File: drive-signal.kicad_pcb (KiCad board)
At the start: 2 copper layers, 43.2 x 67.8 mm, 25 parts, among them J1 Conn_01x03_Pin, J10 Conn_01x04_Pin, J11 Conn_01x04_Pin, J2 Conn_01x03_Pin, J3 Conn_01x03_Pin, J4 Conn_01x03_Pin, J5 JETSON, J6 IMU, J7 Conn_01x02_Pin, J8 Conn_01x04_Pin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

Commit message: fix mount holes
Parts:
- added ?: , , F.Cu at (50.0, 31.5)
- added ?: , , F.Cu at (86.6, 61.2)
- added ?: , , F.Cu at (86.6, 31.5)
- added ?: , , F.Cu at (50.0, 60.7)
- added ?: , , F.Cu at (63.2, 93.0)
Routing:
- net (no net): vias 5 -> 0
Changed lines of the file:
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@@
     )
   )
+  (footprint "" (layer "F.Cu")
+    (at 50.038 31.496)
+    (fp_text reference "" (at 0 0) (layer "F.SilkS")
+        (effects (font (size 1.27 1.27) (thickness 0.15)))
+    )
+    (fp_text value "" (at 0 0) (layer "F.SilkS")
+        (effects (font (size 1.27 1.27) (thickness 0.15)))
+    )
+    (pad "1" thru_hole circle (at 0 0) (size 3.5 3.5) (drill 3.2) (layers "*.Cu" "*.Mask"))
+  )
   (footprint "Resistor_SMD:R_0805_2012Metric_Pad1.20x1.40mm_HandSolder" (layer "F.Cu")
     (at 64.77 62.23 180)
@@
     )
   )
+  (footprint "" (layer "F.Cu")
+    (at 86.614 61.214)
+    (fp_text reference "" (at 0 0) (layer "F.SilkS")
+        (effects (font (size 1.27 1.27) (thickness 0.15)))
+    )
+    (fp_text value "" (at 0 0) (layer "F.SilkS")
+        (effects (font (size 1.27 1.27) (thickness 0.15)))
+    )
+    (pad "1" thru_hole circle (at 0 0) (size 3.5 3.5) (drill 3.2) (layers "*.Cu" "*.Mask"))
+  )
   (footprint "Connector_JST:JST_PH_B3B-PH-K_1x03_P2.00mm_Vertical" (layer "F.Cu")
     (at 84.328 67.422 -90)
@@
     )
   )
+  (footprint "" (layer "F.Cu")
+    (at 86.614 31.496)
+    (fp_text reference "" (at 0 0) (layer "F.SilkS")
+        (effects (font (size 1.27 1.27) (thickness 0.15)))
+    )
+    (fp_text value "" (at 0 0) (layer "F.SilkS")
+        (effects (font (size 1.27 1.27) (thickness 0.15)))
+    )
+    (pad "1" thru_hole circle (at 0 0) (size 3.5 3.5) (drill 3.2) (layers "*.Cu" "*.Mask"))
+  )
   (footprint "LED_SMD:LED_0805_2012Metric_Pad1.15x1.40mm_HandSolder" (layer "F.Cu")
     (at 84.319 46.482 180)
@@
     )
   )
+  (footprint "" (layer "F.Cu")
+    (at 50.038 60.706)
+    (fp_text reference "" (at 0 0) (layer "F.SilkS")
+        (effects (font (size 1.27 1.27) (thickness 0.15)))
+    )
+    (fp_text value "" (at 0 0) (layer "F.SilkS")
+        (effects (font (size 1.27 1.27) (thickness 0.15)))
+    )
+    (pad "1" thru_hole circle (at 0 0) (size 3.5 3.5) (drill 3.2) (layers "*.Cu" "*.Mask"))
+  )
   (footprint "Resistor_SMD:R_0805_2012Metric_Pad1.20x1.40mm_HandSolder" (layer "F.Cu")
     (at 79.97 46.482)
@@
     )
   )
+  (footprint "" (layer "F.Cu")
+    (at 63.246 92.964)
+    (fp_text reference "" (at 0 0) (layer "F.SilkS")
+        (effects (font (size 1.27 1.27) (thickness 0.15)))
+    )
+    (fp_text value "" (at 0 0) (layer "F.SilkS")
+        (effects (font (size 1.27 1.27) (thickness 0.15)))
+    )
+    (pad "1" thru_hole circle (at 0 0) (size 3.5 3.5) (drill 3.2) (layers "*.Cu" "*.Mask"))
+  )
   (footprint "LED_SMD:LED_0805_2012Metric_Pad1.15x1.40mm_HandSolder" (layer "F.Cu")
     (at 84.319 75.438 180)
@@
     (effects (font (size 0.5 0.5) (thickness 0.1)) (justify left bottom))
   )
-  (via (at 63.246 92.964) (size 4) (drill 3.5) (layers "F.Cu" "B.Cu") (free) (net 0))
-  (via (at 86.614 31.496) (size 4) (drill 3.5) (layers "F.Cu" "B.Cu") (free) (net 0))
-  (via (at 50.038 60.706) (size 4) (drill 3.5) (layers "F.Cu" "B.Cu") (free) (net 0))
-  (via (at 86.614 61.214) (size 4) (drill 3.5) (layers "F.Cu" "B.Cu") (free) (net 0))
-  (via (at 50.038 31.496) (size 4) (drill 3.5) (layers "F.Cu" "B.Cu") (free) (net 0))
   (segment (start 59.992 75.438) (end 60.6334 74.7966) (width 1) (layer "F.Cu") (net 7))
   (segment (start 57.404 75.438) (end 57.404 72.373) (width 1) (layer "F.Cu") (net 7))

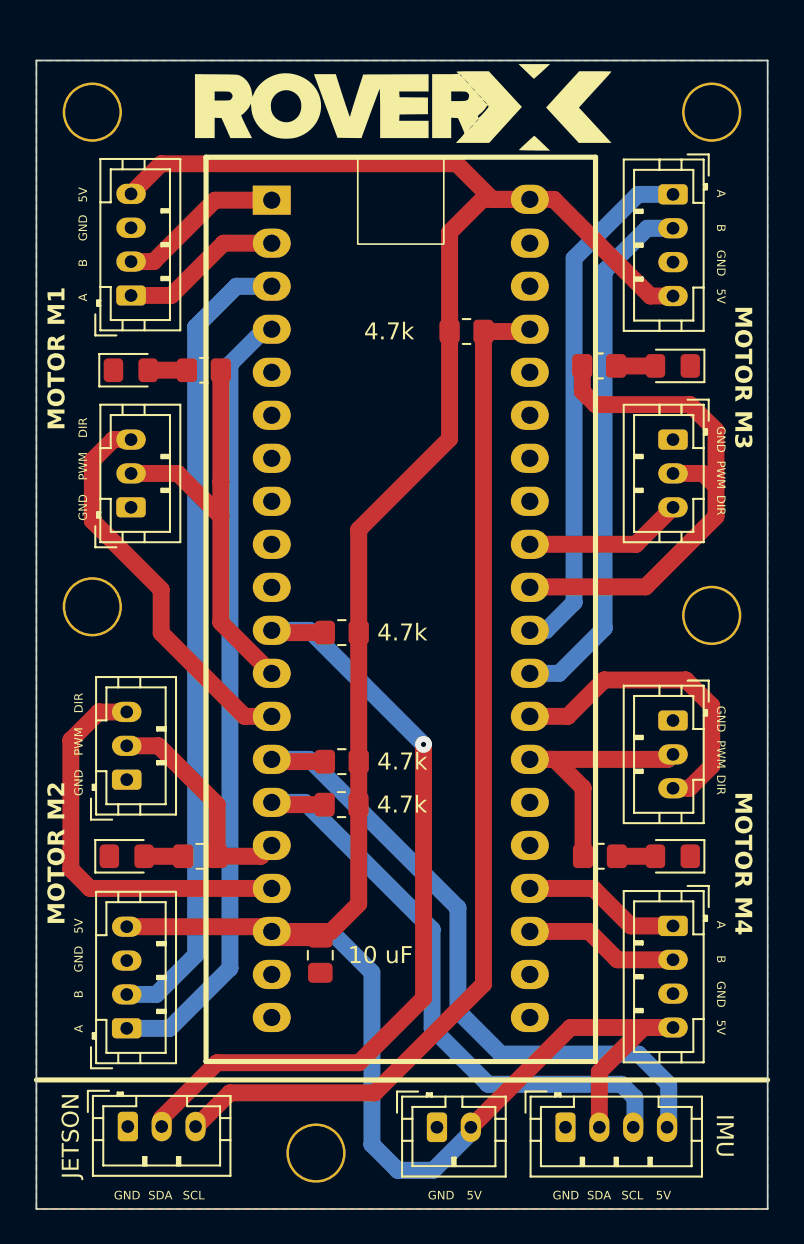
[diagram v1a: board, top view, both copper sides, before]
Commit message: make JSTs horizontal
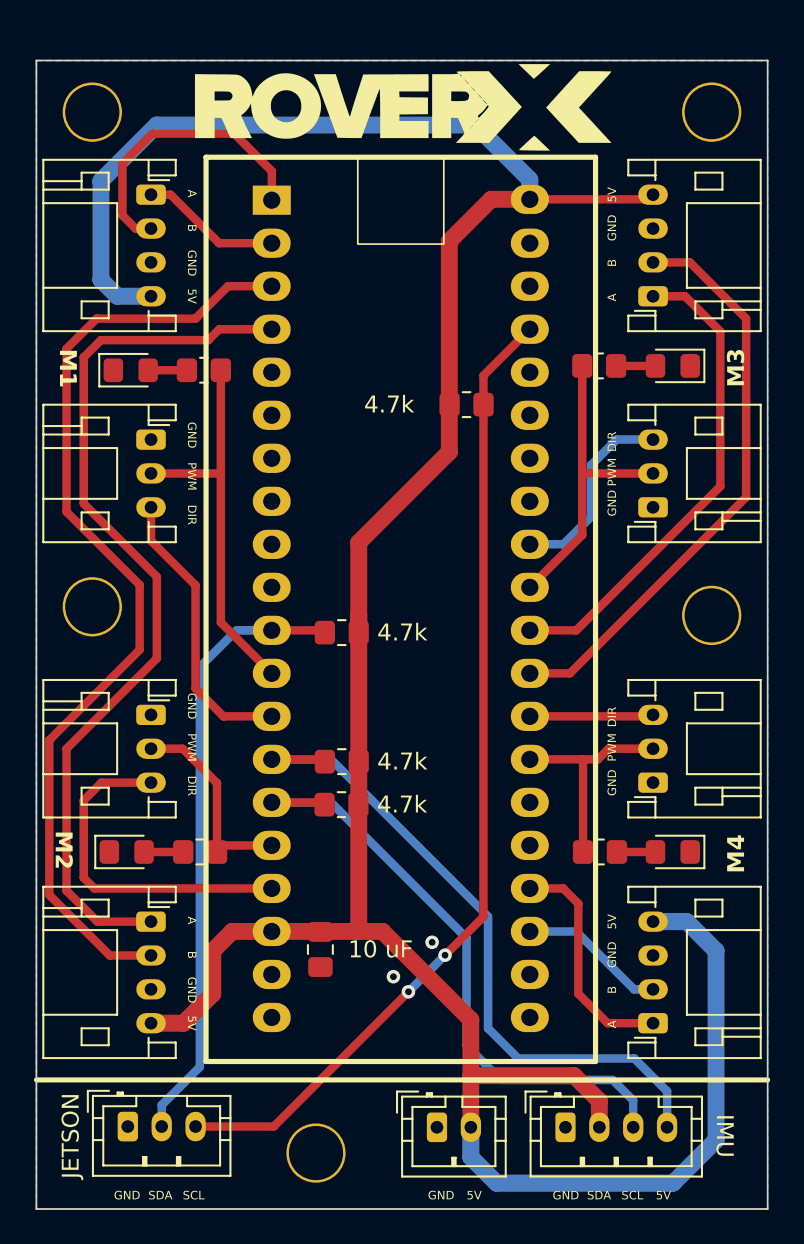
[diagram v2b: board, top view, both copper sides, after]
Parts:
- J1, J2, J3, J4: footprint Connector_JST:JST_PH_B3B-PH-K_1x03_P2.00mm_Vertical -> Connector_JST:JST_PH_S3B-PH-K_1x03_P2.00mm_Horizontal
- J10, J11, J8, J9: footprint Connector_JST:JST_PH_B4B-PH-K_1x04_P2.00mm_Vertical -> Connector_JST:JST_PH_S4B-PH-K_1x04_P2.00mm_Horizontal
- moved J9 6.46 mm to (53.5, 79.3), turned to -90 degrees
- moved J11 6.13 mm to (83.1, 42.4), turned to 90 degrees
- moved J8 6.07 mm to (53.5, 36.4), turned to -90 degrees
- moved J10 5.87 mm to (83.1, 85.3), turned to 90 degrees
- moved R4 4.32 mm to (72.1, 48.8)
- moved J4 4.17 mm to (83.1, 54.8), turned to 90 degrees
- moved J1 4.17 mm to (53.5, 50.8), turned to -90 degrees
- moved J2 4.09 mm to (53.5, 67.1), turned to -90 degrees
- moved J3 3.85 mm to (83.1, 71.1), turned to 90 degrees
- moved C1 0.34 mm to (63.5, 80.9)
- moved D1 0.25 mm to (52.1, 75.2)
- moved D3 0.25 mm to (84.3, 75.2)
- moved R5 0.25 mm to (56.4, 75.2)
- moved R7 0.25 mm to (80.0, 75.2)
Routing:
- net +5V: track 148.8 -> 170.0 mm
- net I2C2_J_SDA: track 49.1 -> 36.4 mm, vias 1 -> 0
- net PWM_RB: track 31.0 -> 18.5 mm
- net DIR_RF: track 19.2 -> 7.31 mm
- net LB_B: track 47.6 -> 57.4 mm
- net LF_B: track 9.81 -> 17.2 mm
- net LB_A: track 46.6 -> 53.0 mm
- net DIR_LF: track 23.2 -> 17.0 mm
- net RF_A: track 9.37 -> 13.7 mm
- net I2C2_J_SCL: track 62.1 -> 58.0 mm, vias 0 -> 2
- net DIR_LB: track 23.9 -> 20.3 mm
- net PWM_RF: track 16.5 -> 13.0 mm
- net RB_B: track 31.7 -> 34.5 mm
- net RB_A: track 31.0 -> 28.8 mm
- net DIR_RB: track 9.36 -> 11.6 mm
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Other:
- board text added: "M1"
- board text added: "M2"
- board text added: "M3"
- board text added: "M4"
- board text removed: "MOTOR M1"
- board text removed: "MOTOR M2"
- board text removed: "MOTOR M3"
- board text removed: "MOTOR M4"

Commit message: minor layout improvements
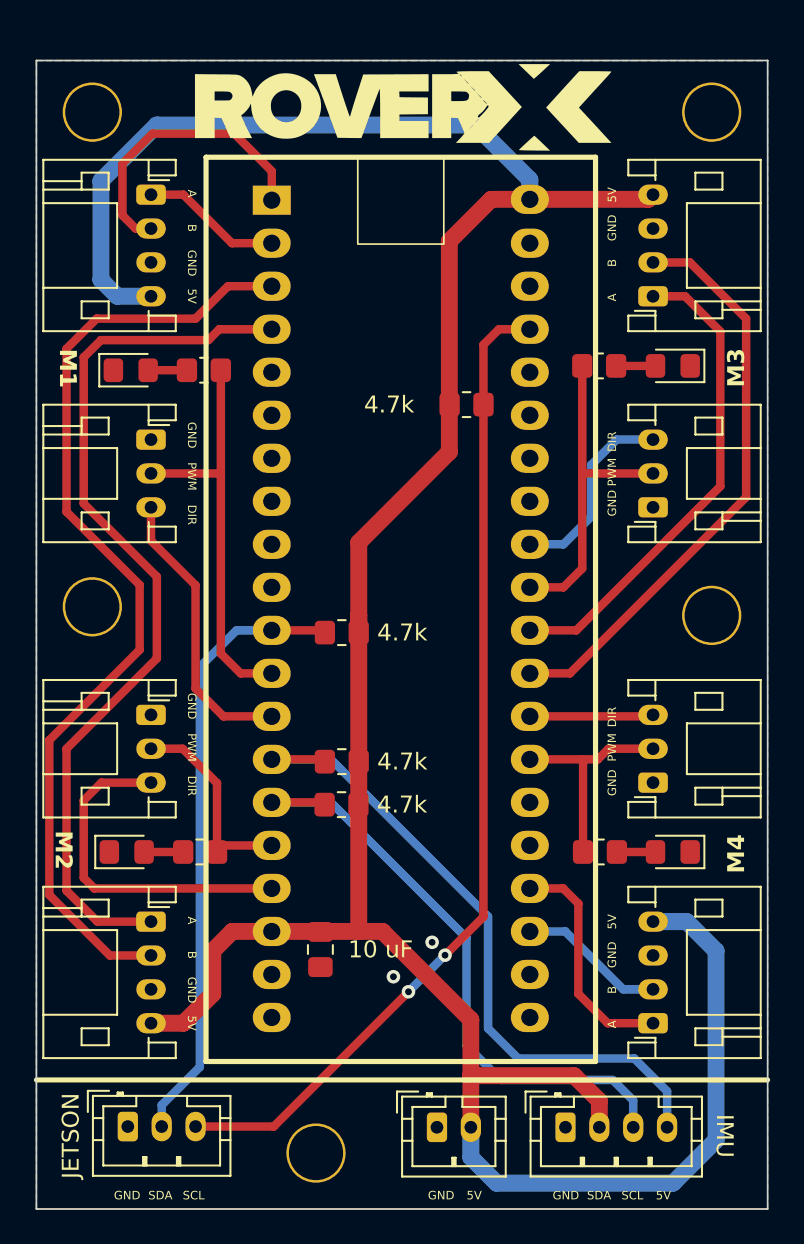
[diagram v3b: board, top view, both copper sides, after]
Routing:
- net PWM_RB: track 18.5 -> 19.7 mm
- net PWM_LF: track 23.3 -> 24.3 mm
- net I2C2_J_SCL: track 58.0 -> 59.0 mm
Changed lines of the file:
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@@
     )
     (stroke (width 0) (type solid)) (fill solid) (layer "F.SilkS"))
-  (gr_line (start 46.736 60.96) (end 46.736 60.96)
-    (stroke (width 0.15) (type default)) (layer "F.SilkS"))
   (gr_poly
     (pts
@@
   (segment (start 53.504 71.088) (end 50.578 71.088) (width 0.5) (layer "F.Cu") (net 8))
   (segment (start 49.53 76.708) (end 50.1586 77.3366) (width 0.5) (layer "F.Cu") (net 8))
-  (segment (start 60.6334 64.6366) (end 57.626 61.6292) (width 0.5) (layer "F.Cu") (net 9))
+  (segment (start 58.7946 64.6366) (end 57.626 63.468) (width 0.5) (layer "F.Cu") (net 9))
+  (segment (start 60.6334 64.6366) (end 58.7946 64.6366) (width 0.5) (layer "F.Cu") (net 9))
   (segment (start 57.626 52.832) (end 57.626 46.736) (width 0.5) (layer "F.Cu") (net 9))
-  (segment (start 57.626 61.6292) (end 57.626 52.832) (width 0.5) (layer "F.Cu") (net 9))
+  (segment (start 57.626 63.468) (end 57.626 52.832) (width 0.5) (layer "F.Cu") (net 9))
   (segment (start 53.504 52.832) (end 57.626 52.832) (width 0.5) (layer "F.Cu") (net 9))
   (segment (start 53.504 56.806) (end 56.134 59.436) (width 0.5) (layer "F.Cu") (net 10))
@@
   (segment (start 71.12 51.562) (end 65.77 56.912) (width 1) (layer "F.Cu") (net 13))
   (segment (start 65.77 79.8606) (end 65.786 79.8766) (width 1) (layer "F.Cu") (net 13))
+  (segment (start 82.8722 36.6458) (end 83.148 36.37) (width 1) (layer "F.Cu") (net 13))
   (segment (start 67.1766 79.8766) (end 65.786 79.8766) (width 1) (layer "F.Cu") (net 13))
-  (segment (start 82.8722 36.6458) (end 83.148 36.37) (width 0.5) (layer "F.Cu") (net 13))
-  (segment (start 75.8734 36.6458) (end 82.8722 36.6458) (width 0.5) (layer "F.Cu") (net 13))
   (segment (start 73.5902 36.6458) (end 71.12 39.116) (width 1) (layer "F.Cu") (net 13))
   (segment (start 72.39 91.44) (end 72.39 88.392) (width 1) (layer "F.Cu") (net 13))
@@
   (segment (start 65.77 56.912) (end 65.77 61.214) (width 1) (layer "F.Cu") (net 13))
   (segment (start 65.77 61.214) (end 65.77 79.8606) (width 1) (layer "F.Cu") (net 13))
+  (segment (start 75.8734 36.6458) (end 82.8722 36.6458) (width 1) (layer "F.Cu") (net 13))
   (segment (start 51.514 42.37) (end 50.546 41.402) (width 1) (layer "B.Cu") (net 13))
   (segment (start 85.138 79.296) (end 86.868 81.026) (width 1) (layer "B.Cu") (net 13))
@@
   (segment (start 79.502 55.372) (end 79.502 52.324) (width 0.5) (layer "B.Cu") (net 18))
   (segment (start 83.148 52.832) (end 78.97 52.832) (width 0.5) (layer "F.Cu") (net 19))
-  (segment (start 75.8734 59.5566) (end 78.97 56.46) (width 0.5) (layer "F.Cu") (net 19))
   (segment (start 78.97 52.832) (end 78.97 46.482) (width 0.5) (layer "F.Cu") (net 19))
-  (segment (start 78.97 56.46) (end 78.97 52.832) (width 0.5) (layer "F.Cu") (net 19))
+  (segment (start 77.8574 59.5566) (end 78.97 58.444) (width 0.5) (layer "F.Cu") (net 19))
+  (segment (start 78.97 58.444) (end 78.97 52.832) (width 0.5) (layer "F.Cu") (net 19))
+  (segment (start 75.8734 59.5566) (end 77.8574 59.5566) (width 0.5) (layer "F.Cu") (net 19))
   (segment (start 75.8734 67.1766) (end 83.0594 67.1766) (width 0.5) (layer "F.Cu") (net 20))
   (segment (start 83.0594 67.1766) (end 83.148 67.088) (width 0.5) (layer "F.Cu") (net 20))
@@
   (segment (start 60.748 91.398) (end 56.134 91.398) (width 0.5) (layer "F.Cu") (net 32))
   (segment (start 68.707 83.439) (end 60.748 91.398) (width 0.5) (layer "F.Cu") (net 32))
-  (segment (start 73.136 47.054) (end 73.136 48.768) (width 0.5) (layer "F.Cu") (net 32))
-  (segment (start 75.8734 44.3166) (end 73.136 47.054) (width 0.5) (layer "F.Cu") (net 32))
+  (segment (start 74.0474 44.3166) (end 73.136 45.228) (width 0.5) (layer "F.Cu") (net 32))
+  (segment (start 75.8734 44.3166) (end 74.0474 44.3166) (width 0.5) (layer "F.Cu") (net 32))
   (segment (start 73.136 48.768) (end 73.136 79.01) (width 0.5) (layer "F.Cu") (net 32))
   (segment (start 73.136 79.01) (end 70.866 81.28) (width 0.5) (layer "F.Cu") (net 32))
+  (segment (start 73.136 45.228) (end 73.136 48.768) (width 0.5) (layer "F.Cu") (net 32))
   (via (at 68.707 83.439) (size 0.8) (drill 0.4) (layers "F.Cu" "B.Cu") (net 32))
   (via (at 70.866 81.28) (size 0.8) (drill 0.4) (layers "F.Cu" "B.Cu") (net 32))
@@
   (segment (start 72.136 80.264) (end 64.1286 72.2566) (width 0.5) (layer "B.Cu") (net 34))
   (segment (start 64.1286 72.2566) (end 60.6334 72.2566) (width 0.5) (layer "B.Cu") (net 34))
-  (segment (start 53.504 36.37) (end 54.658 36.37) (width 0.5) (layer "F.Cu") (net 35))
-  (segment (start 54.658 36.37) (end 57.5246 39.2366) (width 0.5) (layer "F.Cu") (net 35))
-  (segment (start 57.5246 39.2366) (end 60.6334 39.2366) (width 0.5) (layer "F.Cu") (net 35))
+  (segment (start 58.2866 39.2366) (end 60.6334 39.2366) (width 0.5) (layer "F.Cu") (net 35))
+  (segment (start 55.42 36.37) (end 58.2866 39.2366) (width 0.5) (layer "F.Cu") (net 35))
+  (segment (start 53.504 36.37) (end 55.42 36.37) (width 0.5) (layer "F.Cu") (net 35))
   (segment (start 51.816 34.544) (end 53.594 32.766) (width 0.5) (layer "F.Cu") (net 36))
   (segment (start 51.816 37.592) (end 51.816 34.544) (width 0.5) (layer "F.Cu") (net 36))
@@
   (segment (start 78.74 78.232) (end 78.74 83.566) (width 0.5) (layer "F.Cu") (net 38))
   (segment (start 78.74 83.566) (end 80.47 85.296) (width 0.5) (layer "F.Cu") (net 38))
-  (segment (start 82.026 83.296) (end 78.6066 79.8766) (width 0.5) (layer "B.Cu") (net 39))
-  (segment (start 83.148 83.296) (end 82.026 83.296) (width 0.5) (layer "B.Cu") (net 39))
-  (segment (start 78.6066 79.8766) (end 75.8734 79.8766) (width 0.5) (layer "B.Cu") (net 39))
+  (segment (start 77.9716 79.8766) (end 75.8734 79.8766) (width 0.5) (layer "B.Cu") (net 39))
+  (segment (start 81.391 83.296) (end 77.9716 79.8766) (width 0.5) (layer "B.Cu") (net 39))
+  (segment (start 83.148 83.296) (end 81.391 83.296) (width 0.5) (layer "B.Cu") (net 39))
   (segment (start 85.042 42.37) (end 87.122 44.45) (width 0.5) (layer "F.Cu") (net 40))
   (segment (start 83.148 42.37) (end 85.042 42.37) (width 0.5) (layer "F.Cu") (net 40))
@@
   (zone (net 11) (net_name "GND") (layers "F&B.Cu") (hatch edge 0.5)
     (connect_pads yes (clearance 0.5))
-    (min_thickness 0.25) (filled_areas_thickness no)
+    (min_thickness 0.5) (filled_areas_thickness no)
     (fill yes (thermal_gap 0.5) (thermal_bridge_width 0.5) (smoothing fillet) (radius 1))
     (polygon

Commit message: add mounting holes with pads
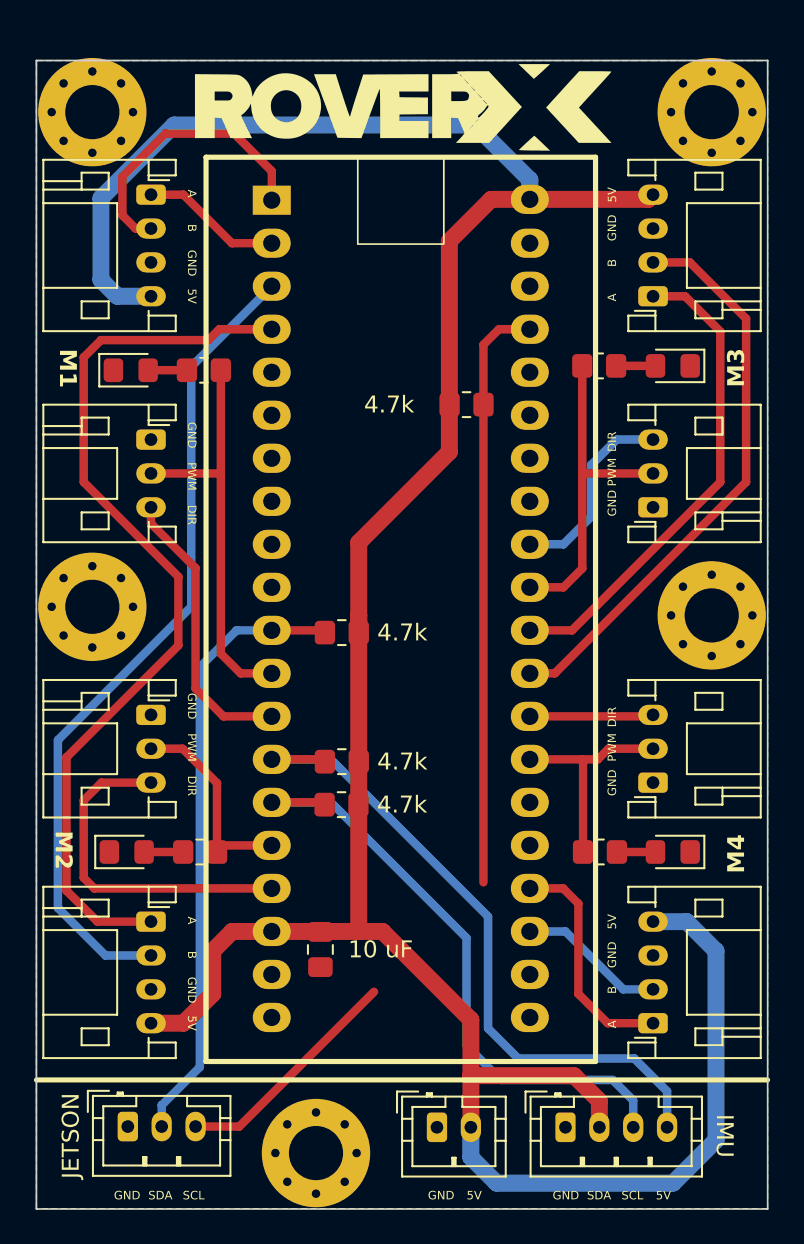
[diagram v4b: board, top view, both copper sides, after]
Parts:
- removed ? (x5): , 
- added H1: MountingHole_Pad, MountingHole:MountingHole_3.2mm_M3_Pad_Via, F.Cu at (86.6, 31.5)
- added H2: MountingHole_Pad, MountingHole:MountingHole_3.2mm_M3_Pad_Via, F.Cu at (50.0, 31.5)
- added H3: MountingHole_Pad, MountingHole:MountingHole_3.2mm_M3_Pad_Via, F.Cu at (50.0, 60.7)
- added H4: MountingHole_Pad, MountingHole:MountingHole_3.2mm_M3_Pad_Via, F.Cu at (86.6, 61.2)
- added H5: MountingHole_Pad, MountingHole:MountingHole_3.2mm_M3_Pad_Via, F.Cu at (63.2, 93.0)
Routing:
- net I2C2_J_SCL: track 59.0 -> 48.7 mm, vias 2 -> 0
- net LB_B: track 57.4 -> 48.6 mm
- net LB_A: track 53.0 -> 54.1 mm
- net +5V: track 170.0 -> 169.4 mm
- net RB_B: track 34.5 -> 34.0 mm
- net GND: vias 2 -> 0
